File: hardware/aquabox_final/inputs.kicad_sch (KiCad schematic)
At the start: 0 parts

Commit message: Atualização
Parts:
- added C3, C4, C5, C6: 100n, symbol Device:C
- added D2, D3, D4, D5, D6, D7: LED, symbol Device:LED
- added J1: Caixa_1, symbol Connector:Screw_Terminal_01x03
- added J3: Caixa_2, symbol Connector:Screw_Terminal_01x03
- added J4: Caixa_3, symbol Connector:Screw_Terminal_01x03
- added R10, R11, R12, R15, R16, R17, R18, R3, R4, R6, R7, R9: 1K, symbol Device:R
- added R13, R14, R19, R20, R21, R22, R23, R24, R5, R8: 10K, symbol Device:R
- added SW1, SW2, SW3, SW4: SW_Push, symbol Switch:SW_Push
- added U3, U4, U5, U6, U7, U8: PC817, Package_DIP:DIP-4_W7.62mm, symbol Isolator:PC817
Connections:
- new net: D6.2 (A), R15.2
- new net: R7.2, U4.1
- new net: R12.2, U6.1
- new net: R11.2, U5.1
- new net: D2.2 (A), R4.2
- new net: D5.2 (A), R10.2
- new net: D3.2 (A), R6.2
- new net: R3.2, U3.1
- new net: R17.2, U7.1
- new net: D4.2 (A), R9.2
- new net: R18.2, U8.1
- new net: D7.2 (A), R16.2
- new net +12V: R10.1, R11.1, R12.1, R15.1, R16.1, R17.1, R18.1, R3.1, R4.1, R6.1, R7.1, R9.1
- new net +3.3V: R13.1, R14.1, R19.1, R20.1, R21.1, R22.1, R23.1, R24.1, R5.1, R8.1
- new net BTN_BACK: C6.1, R24.2, SW4.2
- new net BTN_DOWN: C4.1, R22.2, SW2.2
- new net BTN_ENTER: C5.1, R23.2, SW3.2
- new net BTN_UP: C3.1, R21.2, SW1.2
- new net GND: C3.2, C4.2, C5.2, C6.2, SW1.1, SW2.1, SW3.1, SW4.1, U3.3, U4.3, U5.3, U6.3, U7.3, U8.3
- new net GND1: J1.1 (Pin_1), J3.1 (Pin_1), J4.1 (Pin_1)
- new net LEVEL_HIGH_1: R8.2, U4.4
- new net LEVEL_HIGH_2: R14.2, U6.4
- new net LEVEL_HIGH_3: R20.2, U8.4
- new net LEVEL_LOW_1: R5.2, U3.4
- new net LEVEL_LOW_2: R13.2, U5.4
- new net LEVEL_LOW_3: R19.2, U7.4
- new net SENSOR_H1: D3.1 (K), J1.3 (Pin_3), U4.2
- new net SENSOR_H2: D5.1 (K), J3.3 (Pin_3), U6.2
- new net SENSOR_H3: D7.1 (K), J4.3 (Pin_3), U8.2
- new net SENSOR_L1: D2.1 (K), J1.2 (Pin_2), U3.2
- new net SENSOR_L2: D4.1 (K), J3.2 (Pin_2), U5.2
- new net SENSOR_L3: D6.1 (K), J4.2 (Pin_2), U7.2
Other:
- note added: "GND T1_LOW T1_HIGH"
- company: (none) -> INVENCTUS Soluções Tecnológicas
- title: (none) -> Inputs

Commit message: Atualização
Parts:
- added D8: LED, symbol Device:LED
- added J5: Sensor de Fluxo, symbol Connector:Screw_Terminal_01x03
- added R25, R26: 1K, symbol Device:R
- added R27: 10K, symbol Device:R
- added U9: PC817, Package_DIP:DIP-4_W7.62mm, symbol Isolator:PC817
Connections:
- net +12V: now also J5.1 (Pin_1), R25.1, R26.1
- net +3.3V: now also R27.1
- net GND: now also U9.3
- net GND1: now also J5.3 (Pin_3)
- new net: R26.2, U9.1
- new net: D8.2 (A), R25.2
- new net FLOW_COUNTER: R27.2, U9.4
- new net FLOW_SENSOR: D8.1 (K), J5.2 (Pin_2), U9.2
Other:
- note added: "GND_12V"
- note added: "T1_HIGH"
- note added: "T1_LOW"
- note added: "T2_HIGH"
- note added: "T2_LOW"
- note added: "T3_HIGH"
- note added: "T3_LOW"
- note removed: "GND T1_LOW T1_HIGH"
- moved on the sheet: C3, C4, C5, C6, J1, J3, J4, R21, R22, R23, R24, SW1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

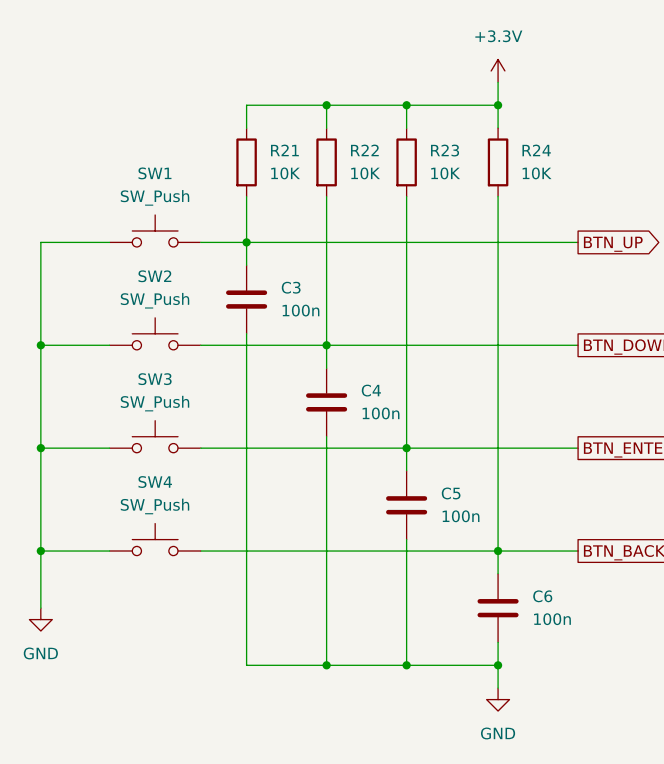
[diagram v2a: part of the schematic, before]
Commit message: Conector do display e teclado
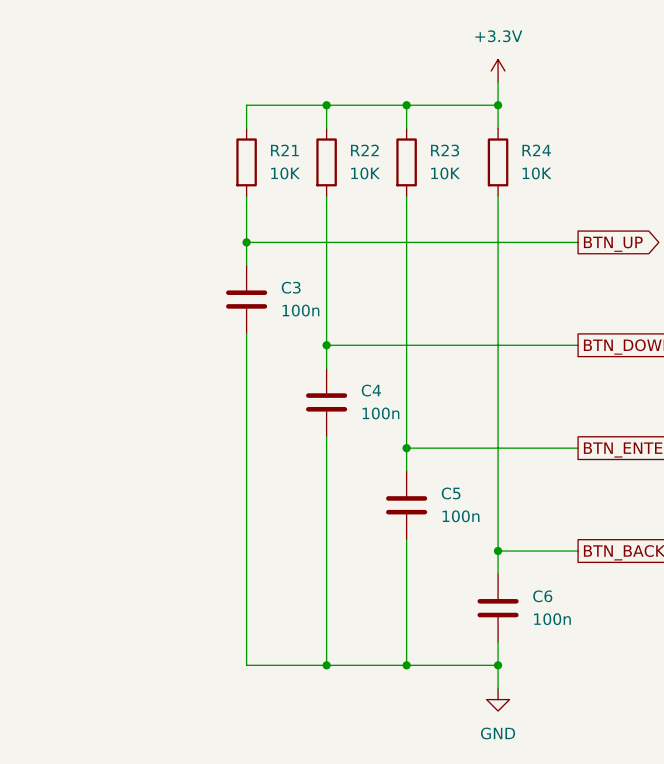
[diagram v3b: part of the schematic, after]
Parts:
- removed SW1, SW2, SW3, SW4: SW_Push, symbol Switch:SW_Push

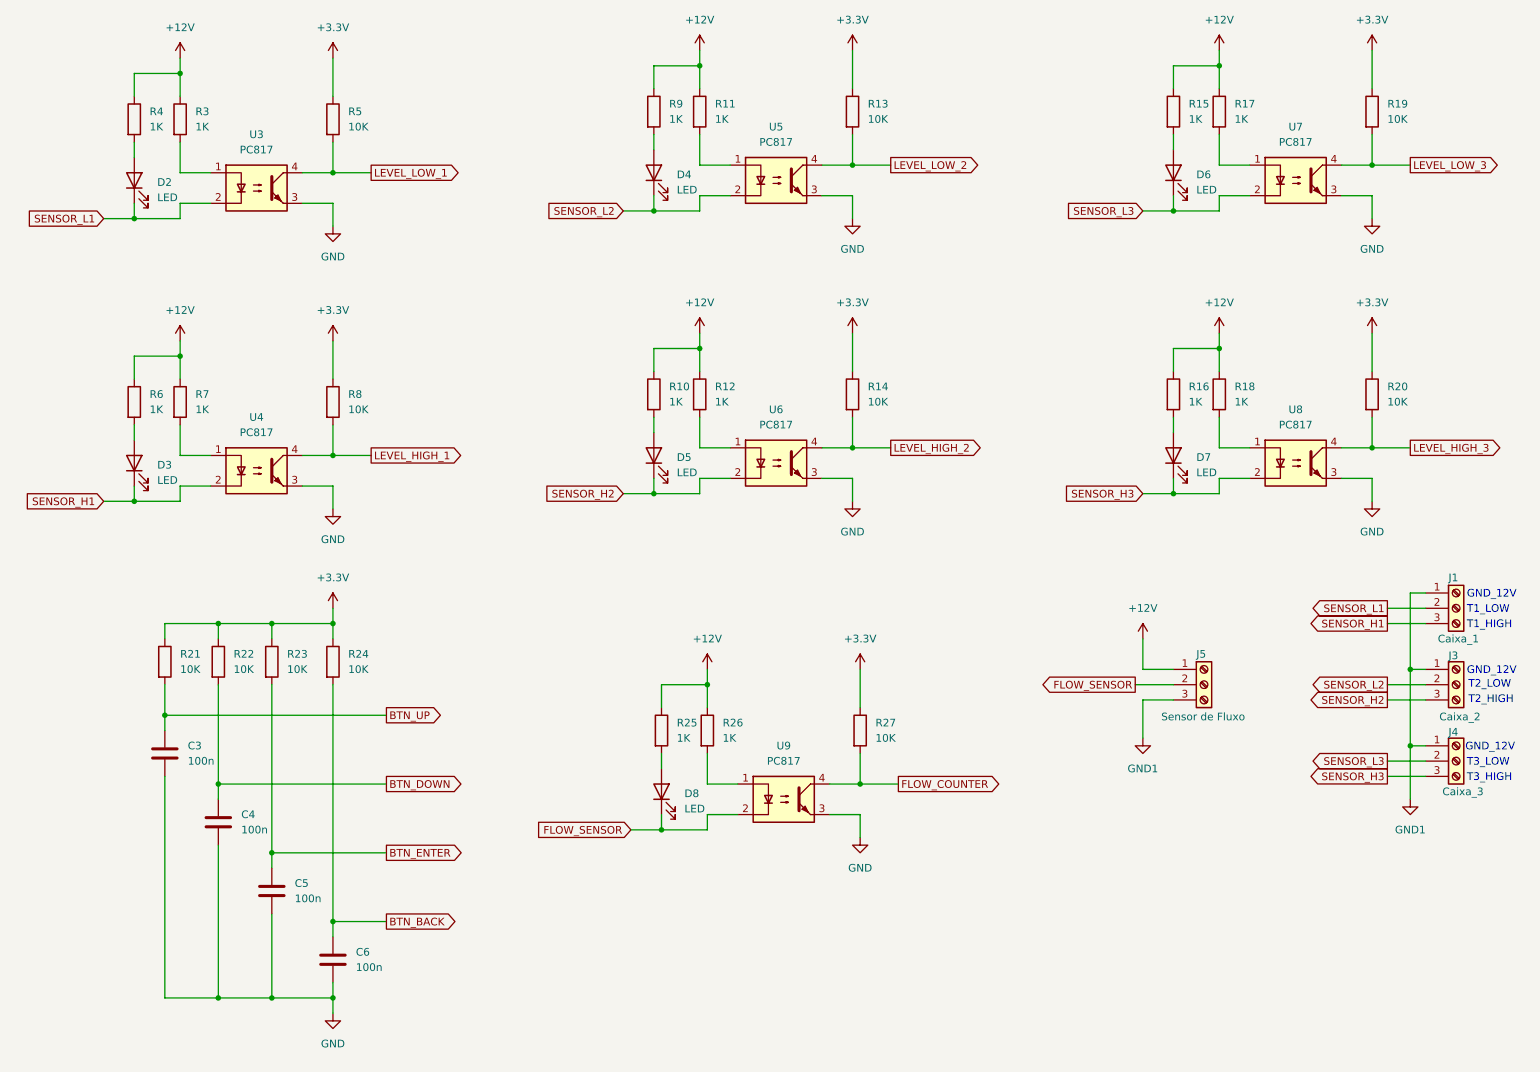
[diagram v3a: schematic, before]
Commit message: Acionamento da bom e solenóides
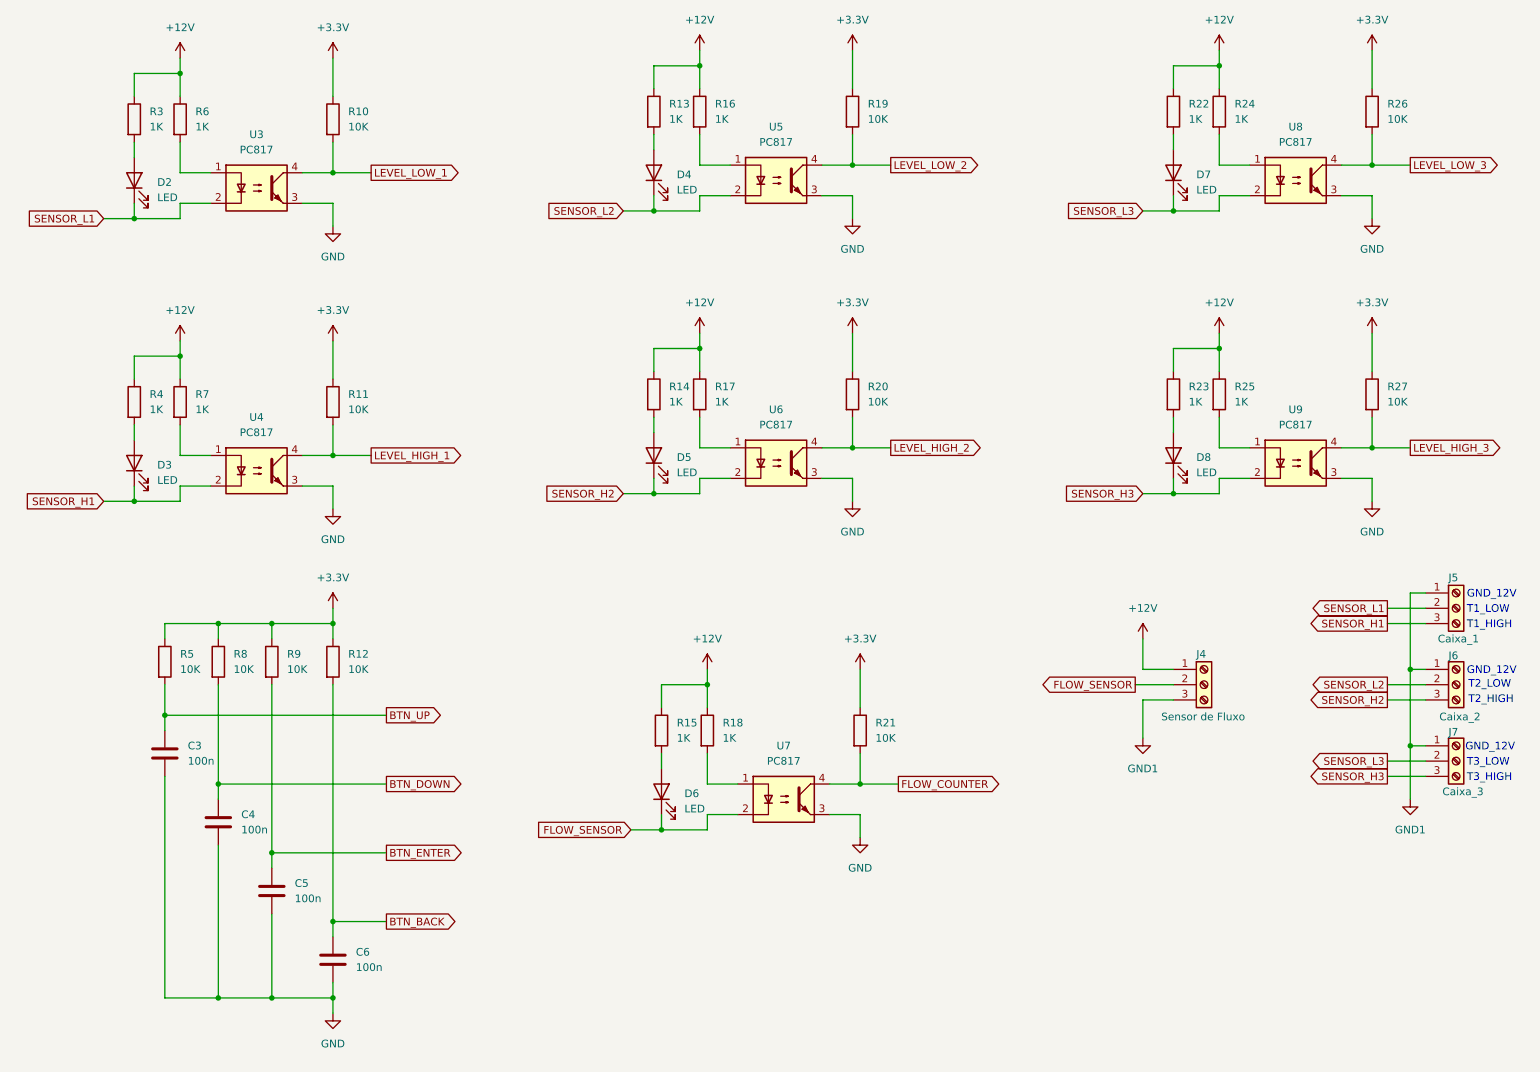
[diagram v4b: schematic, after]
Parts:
- renumbered D8 to D6, D6 to D7, D7 to D8, J5 to J4, J1 to J5, J3 to J6, J4 to J7, R5 to R10, R8 to R11, R24 to R12, R9 to R13, R10 to R14, R25 to R15, R11 to R16, R12 to R17, R26 to R18, R13 to R19, R14 to R20, R27 to R21, R15 to R22, R16 to R23, R17 to R24, R18 to R25, R19 to R26, R20 to R27, R4 to R3, R6 to R4, R21 to R5, R3 to R6, R22 to R8, R23 to R9, U9 to U7, U7 to U8, U8 to U9

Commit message: Atualização
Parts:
- removed C3, C4, C5, C6: 100n, symbol Device:C
- removed R12, R5, R8, R9: 10K, symbol Device:R
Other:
- note added: "GND_+12V"
- note added: "OUT_+12V"
- note added: "SIGNAL"
- note removed: "GND_12V"
- moved on the sheet: D6, J4, J5, J6, J7, R15, R18, R21, U7

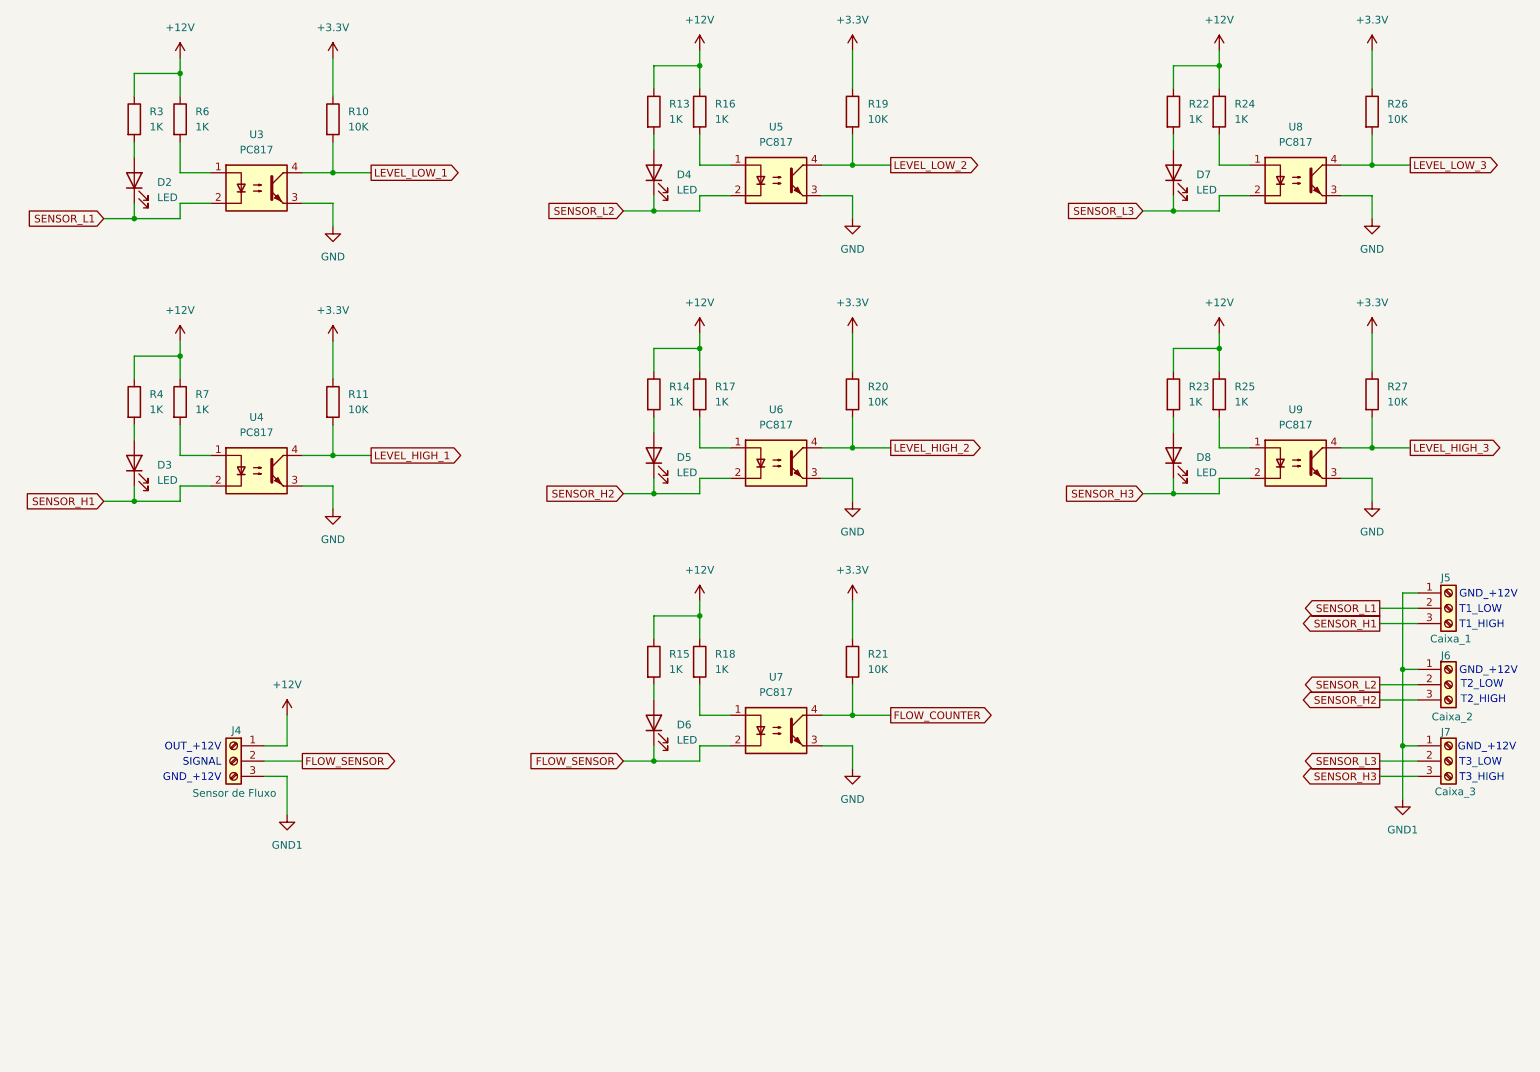
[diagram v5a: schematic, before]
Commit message: Implementação do RTC
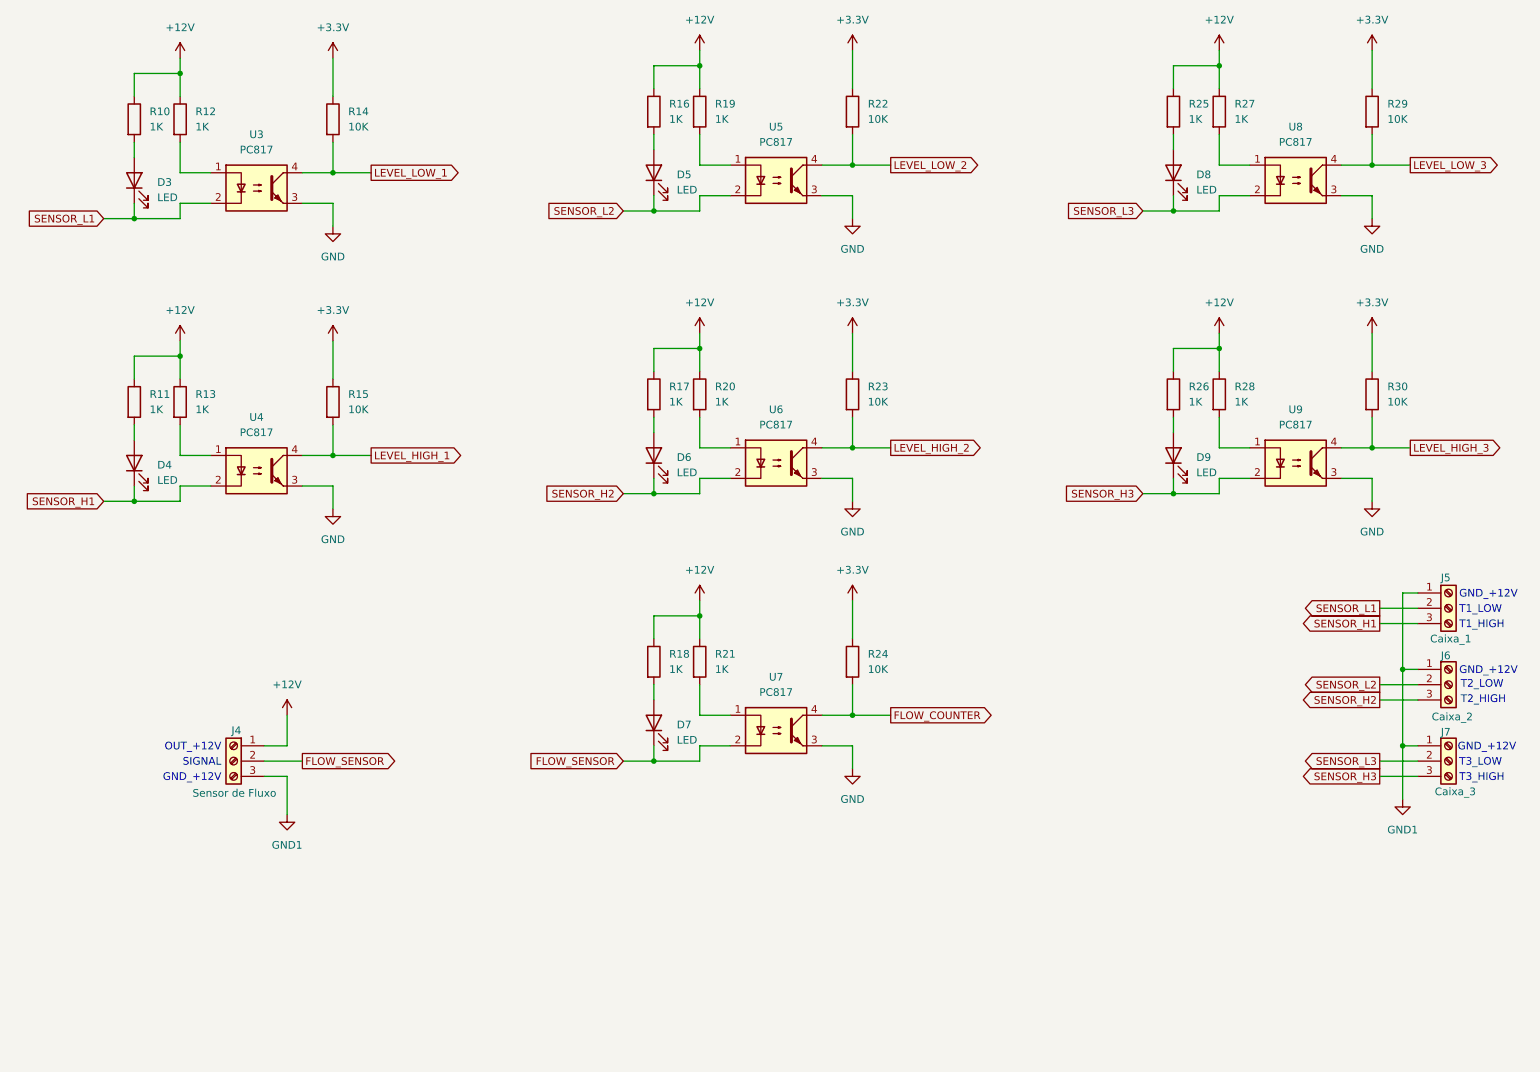
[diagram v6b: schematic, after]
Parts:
- renumbered D2 to D3, D3 to D4, D4 to D5, D5 to D6, D6 to D7, D7 to D8, D8 to D9, R3 to R10, R4 to R11, R6 to R12, R7 to R13, R10 to R14, R11 to R15, R13 to R16, R14 to R17, R15 to R18, R16 to R19, R17 to R20, R18 to R21, R19 to R22, R20 to R23, R21 to R24, R22 to R25, R23 to R26, R24 to R27, R25 to R28, R26 to R29, R27 to R30

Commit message: Atualização
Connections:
- net LEVEL_HIGH_1 renamed T1_HIGH
- net LEVEL_HIGH_2 renamed T2_HIGH
- net LEVEL_HIGH_3 renamed T3_HIGH
- net LEVEL_LOW_1 renamed T1_LOW
- net LEVEL_LOW_2 renamed T2_LOW
- net LEVEL_LOW_3 renamed T3_LOW
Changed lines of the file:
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@@
 		)
 	)
-	(global_label "LEVEL_LOW_2"
+	(global_label "T2_LOW"
 		(shape output)
 		(at 166.37 46.99 0)
@@
 		)
 	)
-	(global_label "LEVEL_HIGH_3"
+	(global_label "T3_HIGH"
 		(shape output)
 		(at 252.73 93.98 0)
@@
 		)
 	)
-	(global_label "LEVEL_LOW_3"
+	(global_label "T3_LOW"
 		(shape output)
 		(at 252.73 46.99 0)
@@
 		)
 	)
-	(global_label "LEVEL_HIGH_1"
+	(global_label "T1_HIGH"
 		(shape output)
 		(at 80.01 95.25 0)
@@
 		)
 	)
-	(global_label "LEVEL_LOW_1"
+	(global_label "T1_LOW"
 		(shape output)
 		(at 80.01 48.26 0)
@@
 		)
 	)
-	(global_label "LEVEL_HIGH_2"
+	(global_label "T2_HIGH"
 		(shape output)
 		(at 166.37 93.98 0)
